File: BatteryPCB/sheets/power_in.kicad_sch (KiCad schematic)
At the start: 9 parts, among them SW1 CAM POWER

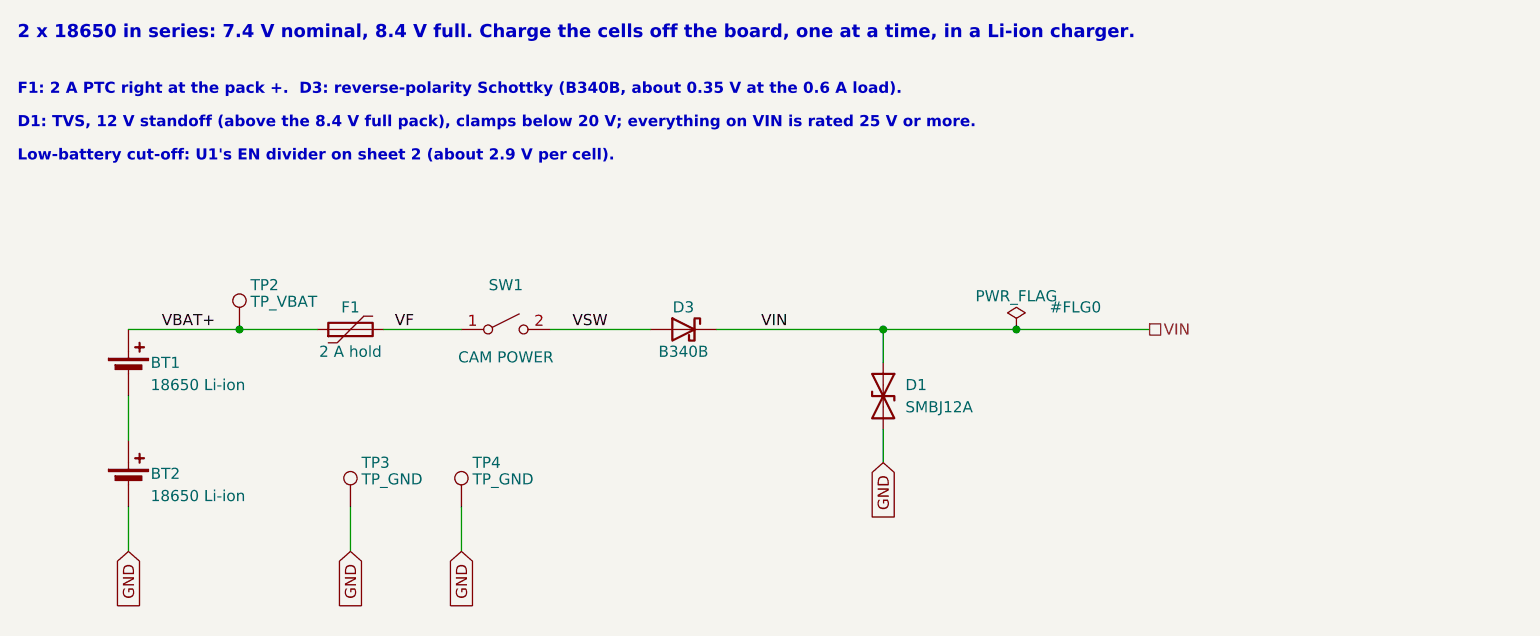
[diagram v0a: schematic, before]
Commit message: Preserve battery PCB progress and prepare partial JLC assembly files
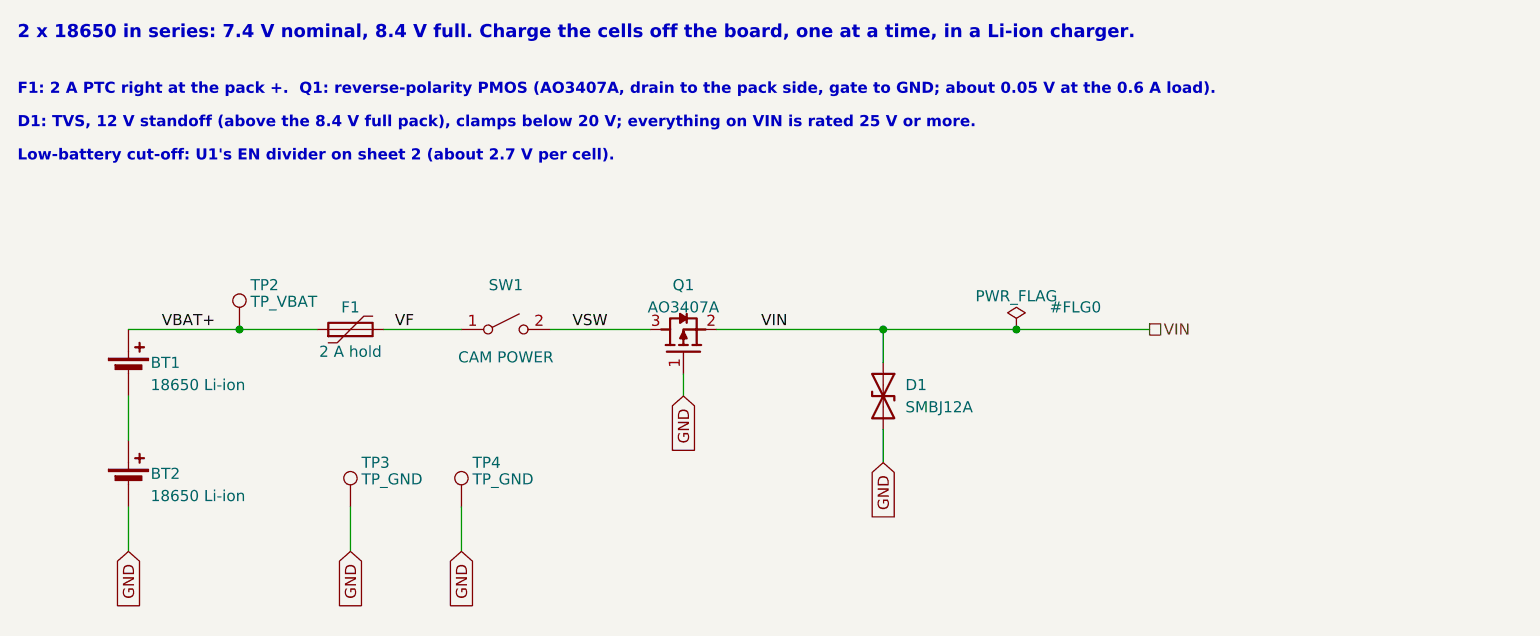
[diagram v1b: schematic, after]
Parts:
- Q1: renamed from D3; value B340B -> AO3407A; footprint Diode_SMD:D_SMB -> Package_TO_SOT_SMD:SOT-23-3; symbol Device:D_Schottky -> battery_pcb:AO3407A; MPN B340B-13-F -> AO3407A; Manufacturer Diodes Incorporated -> Alpha & Omega Semiconductor
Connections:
- net GND: now also Q1.1 (G)
- net VIN: now also Q1.2 (S); no longer Q1.1 (K)
- net VSW: now also Q1.3 (D); no longer Q1.2 (A)
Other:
- note added: "F1: 2 A PTC right at the pack +. Q1: reverse-polarity PMOS (AO3407A, drain to the pack side, gate to GND; about 0.05 V at the 0.6 A load)."
- note added: "Low-battery cut-off: U1's EN divider on sheet 2 (about 2.7 V per cell)."
- note removed: "F1: 2 A PTC right at the pack +. D3: reverse-polarity Schottky (B340B, about 0.35 V at the 0.6 A load)."
- note removed: "Low-battery cut-off: U1's EN divider on sheet 2 (about 2.9 V per cell)."
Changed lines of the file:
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@@
 		)
 	)
-	(text "Low-battery cut-off: U1's EN divider on sheet 2 (about 2.9 V per cell)."
+	(text "Low-battery cut-off: U1's EN divider on sheet 2 (about 2.7 V per cell)."
 		(exclude_from_sim no)
 		(at 25.4 44.45 0)
@@
 		)
 	)
-	(text "F1: 2 A PTC right at the pack +.  D3: reverse-polarity Schottky (B340B, about 0.35 V at the 0.6 A load)."
+	(text "F1: 2 A PTC right at the pack +.  Q1: reverse-polarity PMOS (AO3407A, drain to the pack side, gate to GND; about 0.05 V at the 0.6 A load)."
 		(exclude_from_sim no)
 		(at 25.4 36.83 0)
@@
 		)
 	)
+	(wire
+		(pts
+			(xy 101.6 68.58) (xy 101.6 71.12)
+		)
+		(stroke
+			(width 0)
+			(type default)
+		)
+	)
+	(global_label "GND"
+		(shape input)
+		(at 101.6 71.12 270)
+		(fields_autoplaced yes)
+		(effects
+			(font
+				(size 1.27 1.27)
+			)
+			(justify right)
+		)
+		(property "Intersheetrefs" "${INTERSHEET_REFS}"
+			(at 101.6 71.12 0)
+			(hide yes)
+			(show_name no)
+			(do_not_autoplace no)
+			(effects
+				(font
+					(size 1.27 1.27)
+				)
+			)
+		)
+	)
 	(global_label "GND"
 		(shape input)
@@
 	)
 	(symbol
-		(lib_id "Device:D_Schottky")
+		(lib_id "battery_pcb:AO3407A")
 		(at 101.6 63.5 0)
-		(mirror y)
 		(unit 1)
 		(body_style 1)
@@
 		(in_pos_files yes)
 		(dnp no)
-		(fields_autoplaced yes)
-		(property "Reference" "D3"
+		(property "Reference" "Q1"
+			(at 101.6 58.42 0)
+			(show_name no)
+			(do_not_autoplace no)
+			(effects
+				(font
+					(size 1.27 1.27)
+				)
+			)
+		)
+		(property "Value" "AO3407A"
 			(at 101.6 60.96 0)
 			(show_name no)
@@
 			)
 		)
-		(property "Value" "B340B"
-			(at 101.6 66.04 0)
-			(show_name no)
-			(do_not_autoplace no)
-			(effects
-				(font
-					(size 1.27 1.27)
-				)
-			)
-		)
-		(property "Footprint" "Diode_SMD:D_SMB"
+		(property "Footprint" "Package_TO_SOT_SMD:SOT-23-3"
 			(at 101.6 63.5 0)
 			(hide yes)
@@
 			)
 		)
-		(property "Datasheet" ""
+		(property "Datasheet" "https://www.aosmd.com/res/datasheets/AO3407A.pdf"
 			(at 101.6 63.5 0)
 			(hide yes)
@@
 			)
 		)
-		(property "Description" ""
+		(property "Description" "Reverse-polarity PMOS: drain to the pack side (VSW), source to VIN, gate to GND"
 			(at 101.6 63.5 0)
-			(show_name no)
-			(do_not_autoplace no)
-			(effects
-				(font
-					(size 1.27 1.27)
-				)
-			)
-		)
-		(property "Manufacturer" "Diodes Incorporated"
+			(hide yes)
+			(show_name no)
+			(do_not_autoplace no)
+			(effects
+				(font
+					(size 1.27 1.27)
+				)
+			)
+		)
+		(property "Manufacturer" "Alpha & Omega Semiconductor"
 			(at 101.6 63.5 0)
 			(hide yes)
@@
 			)
 		)
-		(property "MPN" "B340B-13-F"
+		(property "MPN" "AO3407A"
 			(at 101.6 63.5 0)
 			(hide yes)
@@
 		)
 		(pin "2"
+		)
+		(pin "3"
 		)
 		(instances
 			(project "battery_pcb"
 				(path "/19ef3a32-de7c-46ee-a850-2420f6d47f94/ae01c8e7-4191-4202-a535-afc32959794b"
-					(reference "D3")
+					(reference "Q1")
 					(unit 1)
 				)
